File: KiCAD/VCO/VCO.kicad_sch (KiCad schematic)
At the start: 40 parts, among them J1 CV IN 1, J2 CV IN 2, J3 PWM, J4 SAW OUT, J5 PULSE OUT, J6 Conn_01x03_Pin, J7 Conn_01x03_Pin, Q1 NPN, T1 PNP, T2 NPN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

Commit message: Make the transistors touch
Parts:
- Q1: footprint Package_TO_SOT_THT:TO-92L_Inline -> HackSynth:TO-92_Inline - Handsolder
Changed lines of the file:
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@@
 			)
 		)
-		(property "Footprint" "Package_TO_SOT_THT:TO-92L_Inline"
+		(property "Footprint" "HackSynth:TO-92_Inline - Handsolder"
 			(at 177.8 151.13 0)
 			(effects

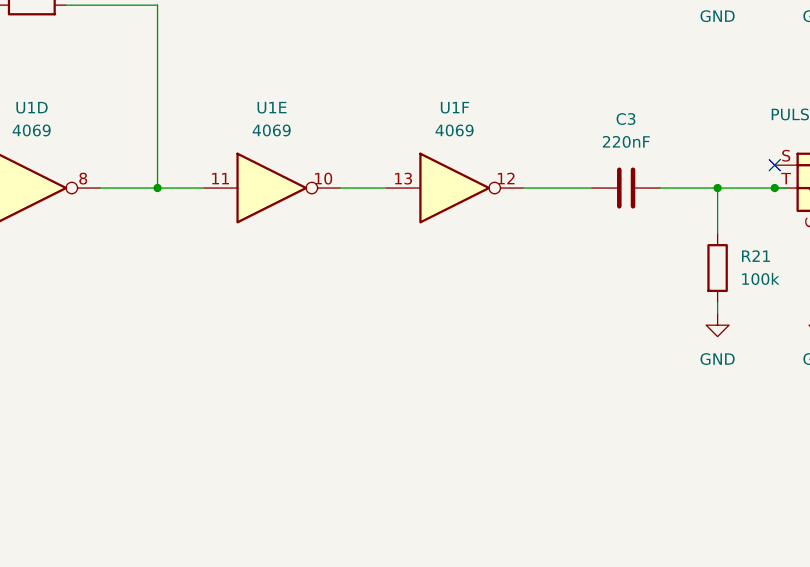
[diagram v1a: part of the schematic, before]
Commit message: Add a cap to pin 13
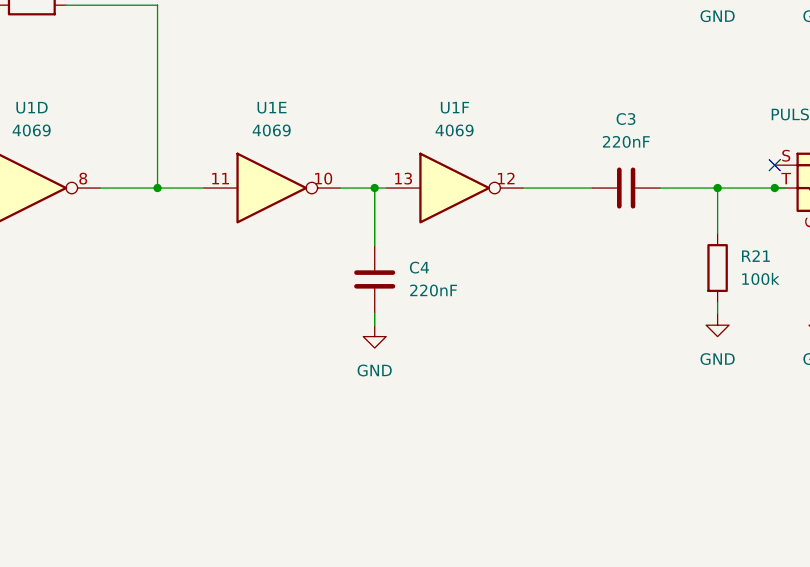
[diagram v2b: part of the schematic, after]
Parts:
- added C4: 220nF, Capacitor_THT:C_Disc_D5.0mm_W2.5mm_P2.50mm, symbol Device:C
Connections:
- net GND: now also C4.1
- net at U1.10, U1.13: now also C4.2
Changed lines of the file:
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@@
 	)
 	(junction
+		(at 210.82 140.97)
+		(diameter 0)
+		(color 0 0 0 0)
+	)
+	(junction
 		(at 144.78 54.61)
 		(diameter 0)
@@
 	(wire
 		(pts
+			(xy 210.82 140.97) (xy 210.82 147.32)
+		)
+		(stroke
+			(width 0)
+			(type default)
+		)
+	)
+	(wire
+		(pts
 			(xy 260.35 69.85) (xy 246.38 69.85)
 		)
@@
 	(wire
 		(pts
-			(xy 212.09 140.97) (xy 207.01 140.97)
+			(xy 212.09 140.97) (xy 210.82 140.97)
 		)
 		(stroke
@@
 	(wire
 		(pts
+			(xy 210.82 140.97) (xy 207.01 140.97)
+		)
+		(stroke
+			(width 0)
+			(type default)
+		)
+	)
+	(wire
+		(pts
 			(xy 176.53 120.65) (xy 186.69 120.65)
 		)
@@
 	(wire
 		(pts
+			(xy 210.82 156.21) (xy 210.82 154.94)
+		)
+		(stroke
+			(width 0)
+			(type default)
+		)
+	)
+	(wire
+		(pts
 			(xy 260.35 39.37) (xy 246.38 39.37)
 		)
@@
 	)
 	(symbol
+		(lib_id "Device:C")
+		(at 210.82 151.13 180)
+		(unit 1)
+		(exclude_from_sim no)
+		(in_bom yes)
+		(on_board yes)
+		(dnp no)
+		(fields_autoplaced yes)
+		(property "Reference" "C4"
+			(at 214.63 149.8599 0)
+			(effects
+				(font
+					(size 1.27 1.27)
+				)
+				(justify right)
+			)
+		)
+		(property "Value" "220nF"
+			(at 214.63 152.3999 0)
+			(effects
+				(font
+					(size 1.27 1.27)
+				)
+				(justify right)
+			)
+		)
+		(property "Footprint" "Capacitor_THT:C_Disc_D5.0mm_W2.5mm_P2.50mm"
+			(at 209.8548 147.32 0)
+			(effects
+				(font
+					(size 1.27 1.27)
+				)
+				(hide yes)
+			)
+		)
+		(property "Datasheet" "~"
+			(at 210.82 151.13 0)
+			(effects
+				(font
+					(size 1.27 1.27)
+				)
+				(hide yes)
+			)
+		)
+		(property "Description" "Unpolarized capacitor"
+			(at 210.82 151.13 0)
+			(effects
+				(font
+					(size 1.27 1.27)
+				)
+				(hide yes)
+			)
+		)
+		(pin "1"
+		)
+		(pin "2"
+		)
+		(instances
+			(project "VCO"
+				(path "/5da6b9e5-71b4-4d0f-a700-8382e26a6af5"
+					(reference "C4")
+					(unit 1)
+				)
+			)
+		)
+	)
+	(symbol
 		(lib_id "Device:R")
 		(at 71.12 57.15 270)
@@
 					(unit 1)
 				)
+			)
+		)
+	)
+	(symbol
+		(lib_id "power:GND")
+		(at 210.82 156.21 0)
+		(unit 1)
+		(exclude_from_sim no)
+		(in_bom yes)
+		(on_board yes)
+		(dnp no)
+		(property "Reference" "#PWR027"
+			(at 210.82 162.56 0)
+			(effects
+				(font
+					(size 1.27 1.27)
+				)
+				(hide yes)
+			)
+		)
+		(property "Value" "GND"
+			(at 210.82 161.29 0)
+			(effects
+				(font
+					(size 1.27 1.27)
+				)
+			)
+		)
+		(property "Footprint" ""
+			(at 210.82 156.21 0)
+			(effects
+				(font
+					(size 1.27 1.27)
+				)
+				(hide yes)
+			)
+		)
+		(property "Datasheet" ""
+			(at 210.82 156.21 0)
+			(effects
+				(font
+					(size 1.27 1.27)
+				)
+				(hide yes)
+			)
+		)
+		(property "Description" "Power symbol creates a global label with name \"GND\" , ground"
+			(at 210.82 156.21 0)
+			(effects
+				(font
+					(size 1.27 1.27)
+				)
+				(hide yes)
+			)
+		)
+		(pin "1"
+		)
+		(instances
+			(project "VCO"
+				(path "/5da6b9e5-71b4-4d0f-a700-8382e26a6af5"
+					(reference "#PWR027")
+					(unit 1)
+				)

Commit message: Chorus PCB Dread + Footprint Edit
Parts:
- U1: footprint Package_DIP:DIP-14_W7.62mm_LongPads -> HackSynth:DIP-14_W7.62mm_LongPads
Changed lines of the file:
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@@
 			)
 		)
-		(property "Footprint" "Package_DIP:DIP-14_W7.62mm_LongPads"
+		(property "Footprint" "HackSynth:DIP-14_W7.62mm_LongPads"
 			(at 227.33 67.31 0)
 			(effects
@@
 			)
 		)
-		(property "Footprint" "Package_DIP:DIP-14_W7.62mm_LongPads"
+		(property "Footprint" "HackSynth:DIP-14_W7.62mm_LongPads"
 			(at 172.72 140.97 0)
 			(effects
@@
 			)
 		)
-		(property "Footprint" "Package_DIP:DIP-14_W7.62mm_LongPads"
+		(property "Footprint" "HackSynth:DIP-14_W7.62mm_LongPads"
 			(at 199.39 140.97 0)
 			(effects
@@
 			)
 		)
-		(property "Footprint" "Package_DIP:DIP-14_W7.62mm_LongPads"
+		(property "Footprint" "HackSynth:DIP-14_W7.62mm_LongPads"
 			(at 219.71 140.97 0)
 			(effects
@@
 			)
 		)
-		(property "Footprint" "Package_DIP:DIP-14_W7.62mm_LongPads"
+		(property "Footprint" "HackSynth:DIP-14_W7.62mm_LongPads"
 			(at 198.12 71.12 0)
 			(effects
@@
 			)
 		)
-		(property "Footprint" "Package_DIP:DIP-14_W7.62mm_LongPads"
+		(property "Footprint" "HackSynth:DIP-14_W7.62mm_LongPads"
 			(at 179.07 71.12 0)
 			(effects
@@
 			)
 		)
-		(property "Footprint" "Package_DIP:DIP-14_W7.62mm_LongPads"
+		(property "Footprint" "HackSynth:DIP-14_W7.62mm_LongPads"
 			(at 144.78 71.12 0)
 			(effects

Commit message: Backups
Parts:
- renumbered R6 to R1, R4 to R2, R5 to R3, R2 to R4, R3 to R5, R1 to R6
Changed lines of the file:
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@@
 		(dnp no)
 		(fields_autoplaced yes)
-		(property "Reference" "R3"
+		(property "Reference" "R5"
 			(at 59.69 72.39 90)
 			(effects
@@
 			(project ""
 				(path "/5da6b9e5-71b4-4d0f-a700-8382e26a6af5"
-					(reference "R3")
+					(reference "R5")
 					(unit 1)
 				)
@@
 		(dnp no)
 		(fields_autoplaced yes)
-		(property "Reference" "R4"
+		(property "Reference" "R2"
 			(at 71.12 26.67 90)
 			(effects
@@
 			(project ""
 				(path "/5da6b9e5-71b4-4d0f-a700-8382e26a6af5"
-					(reference "R4")
+					(reference "R2")
 					(unit 1)
 				)
@@
 		(dnp no)
 		(fields_autoplaced yes)
-		(property "Reference" "R5"
+		(property "Reference" "R3"
 			(at 71.12 50.8 90)
 			(effects
@@
 			(project ""
 				(path "/5da6b9e5-71b4-4d0f-a700-8382e26a6af5"
-					(reference "R5")
+					(reference "R3")
 					(unit 1)
 				)
@@
 		(dnp no)
 		(fields_autoplaced yes)
-		(property "Reference" "R2"
+		(property "Reference" "R4"
 			(at 59.69 50.8 90)
 			(effects
@@
 			(project ""
 				(path "/5da6b9e5-71b4-4d0f-a700-8382e26a6af5"
-					(reference "R2")
+					(reference "R4")
 					(unit 1)
 				)
@@
 		(dnp no)
 		(fields_autoplaced yes)
-		(property "Reference" "R6"
+		(property "Reference" "R1"
 			(at 71.12 72.39 90)
 			(effects
@@
 			(project ""
 				(path "/5da6b9e5-71b4-4d0f-a700-8382e26a6af5"
-					(reference "R6")
+					(reference "R1")
 					(unit 1)
 				)
@@
 		(dnp no)
 		(fields_autoplaced yes)
-		(property "Reference" "R1"
+		(property "Reference" "R6"
 			(at 59.69 26.67 90)
 			(effects
@@
 			(project ""
 				(path "/5da6b9e5-71b4-4d0f-a700-8382e26a6af5"
-					(reference "R1")
+					(reference "R6")
 					(unit 1)
 				)

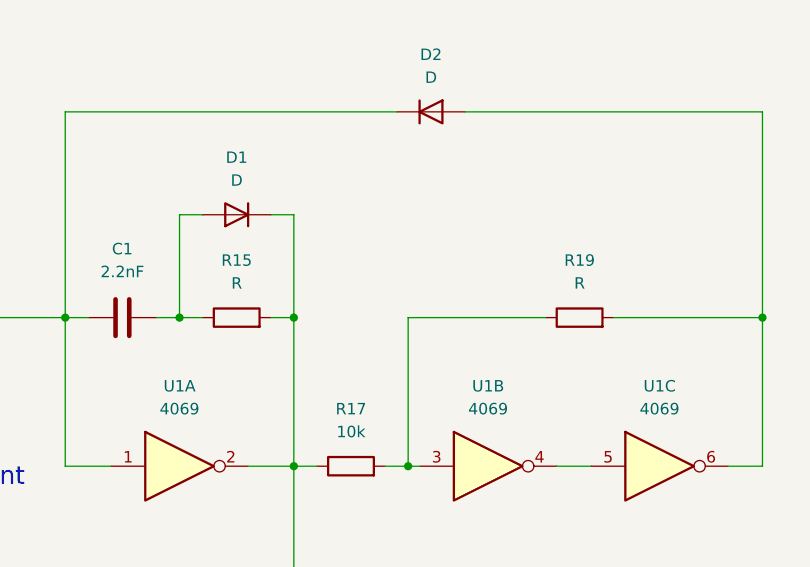
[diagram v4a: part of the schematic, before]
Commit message: Fix missing resistor values
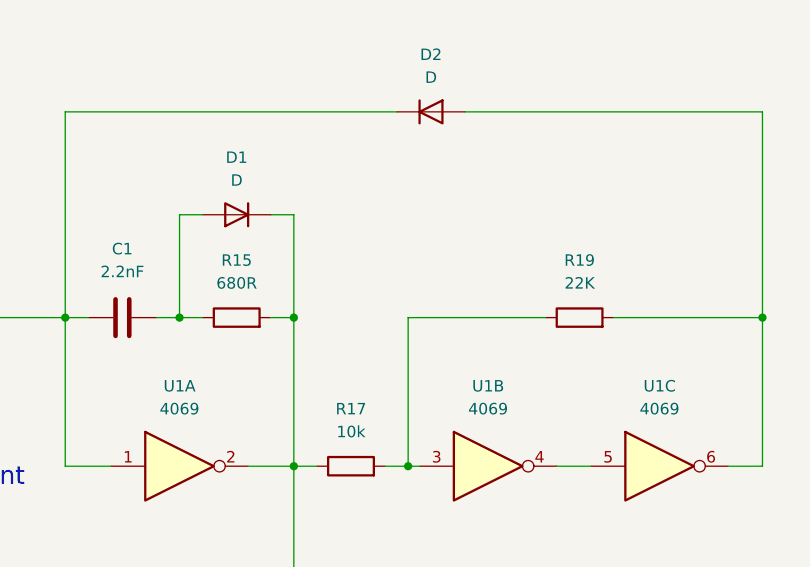
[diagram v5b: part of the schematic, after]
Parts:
- R15: value R -> 680R
- R19: value R -> 22K
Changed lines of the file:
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@@
 			)
 		)
-		(property "Value" "R"
+		(property "Value" "22K"
 			(at 189.23 50.8 90)
 			(effects
@@
 			)
 		)
-		(property "Value" "R"
+		(property "Value" "680R"
 			(at 151.13 50.8 90)
 			(effects
